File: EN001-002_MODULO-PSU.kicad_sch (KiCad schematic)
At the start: 90 parts, among them J1 2x5P 2.54mm, J2 Conn_01x02, J3 Barrel_Jack_Switch, J5 1x3P 2mm, J6 Conn_01x04, Q10 AO3401, Q11 KY6802, Q13 MMBT2222A, Q2 AO3401, Q3 KY6802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

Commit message: schematic minor rearrangments
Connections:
- net DRIVE: now also U2.4; no longer U2.5
- net RESET: now also U2.5; no longer U2.4
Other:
- moved on the sheet: U2B
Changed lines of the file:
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@@
 	(symbol
 		(lib_id "00EN_DB:IC_LOGIC/74HC132D,653")
-		(at 154.94 134.62 180)
+		(at 154.94 134.62 0)
+		(mirror y)
 		(unit 2)
 		(exclude_from_sim no)
@@
 		(dnp no)
 		(property "Reference" "U2"
-			(at 154.94 140.208 0)
+			(at 154.94 129.54 0)
 			(effects
 				(font
@@
 		)
 		(property "Value" "74HC132D,653"
-			(at 154.9483 140.97 0)
+			(at 154.9483 128.27 0)
 			(effects
 				(font
@@
 		)
 		(property "Datasheet" "http://www.ti.com/lit/gpn/sn74LS132"
-			(at 154.94 142.24 0)
+			(at 154.94 127 0)
 			(effects
 				(font
@@
 		)
 		(property "Sim.Library" "/home/fabio/Documents/03_KICAD_DEVELOPEMENT/EN_KICAD_LIBRARY/symbols/NAND_ST.cir"
-			(at 154.94 144.78 0)
+			(at 154.94 124.46 0)
 			(effects
 				(font
@@
 		)
 		(property "Sim.Name" "74HC132"
-			(at 146.05 149.86 0)
+			(at 146.05 119.38 0)
 			(effects
 				(font
@@
 		)
 		(property "Sim.Device" "SUBCKT"
-			(at 156.21 149.86 0)
+			(at 156.21 119.38 0)
 			(effects
 				(font
@@
 		)
 		(property "Sim.Pins" "1=1A 2=1B 3=1OUT 4=2A 5=2B 6=2OUT 7=AGND 8=3OUT 9=3A 10=3B 11=4OUT 12=4A 13=5B 14=VCC"
-			(at 153.67 147.32 0)
+			(at 153.67 121.92 0)
 			(effects
 				(font

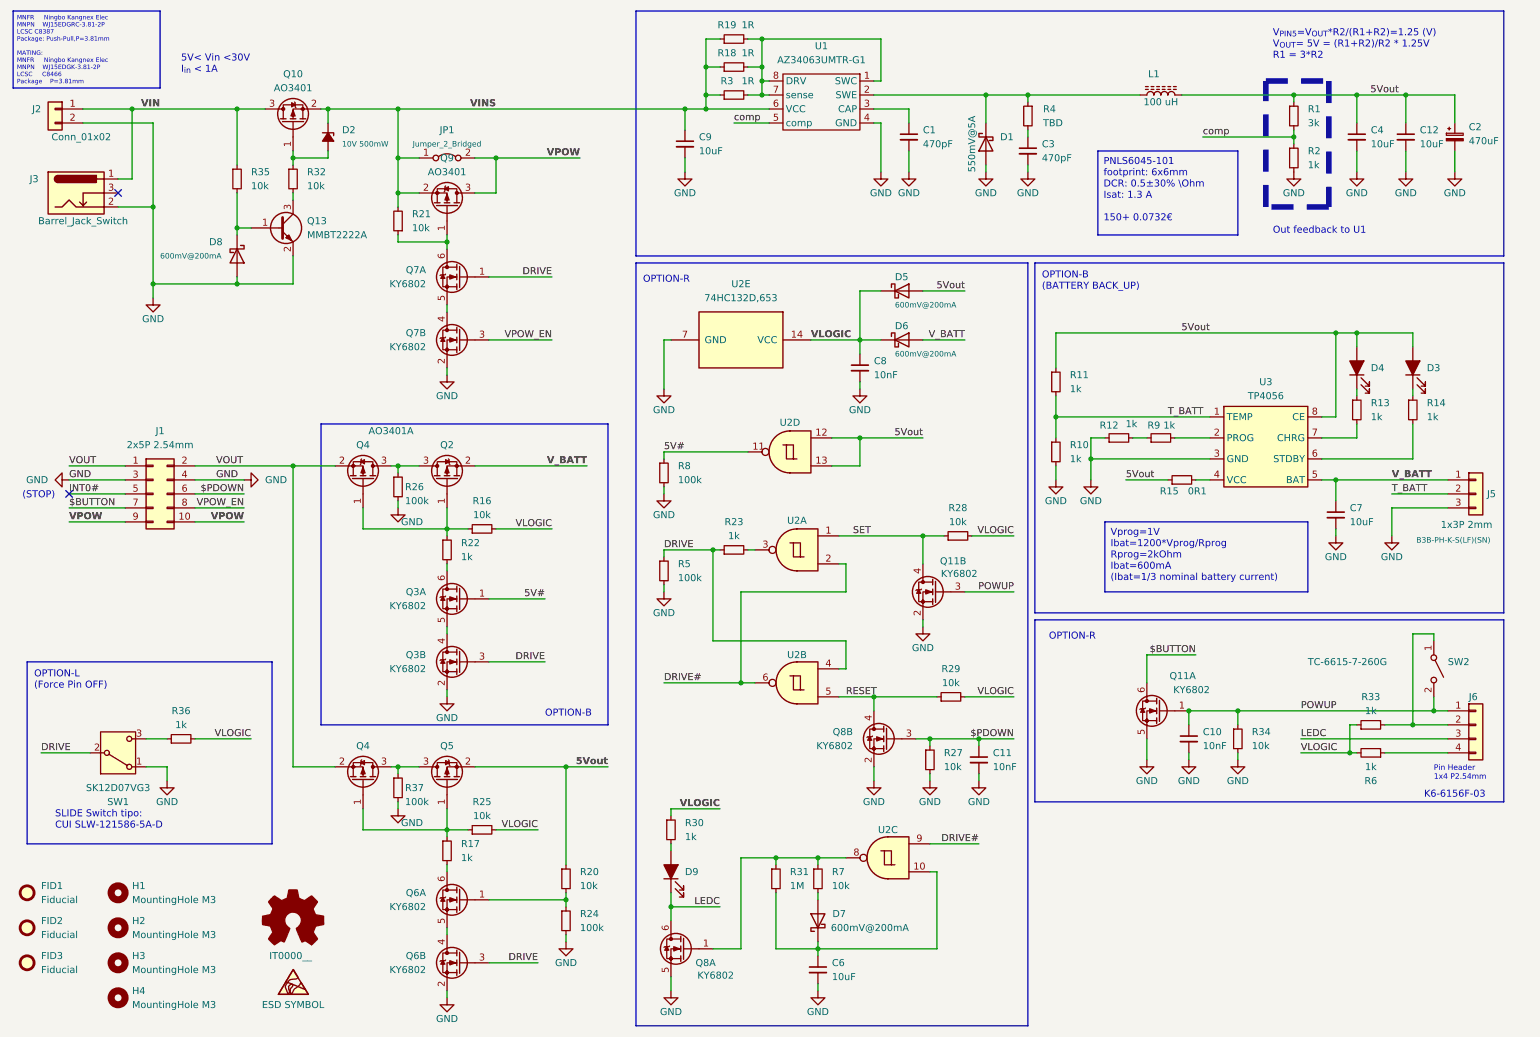
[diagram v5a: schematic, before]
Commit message: Adde Q12 to drive power-up from microcontroller
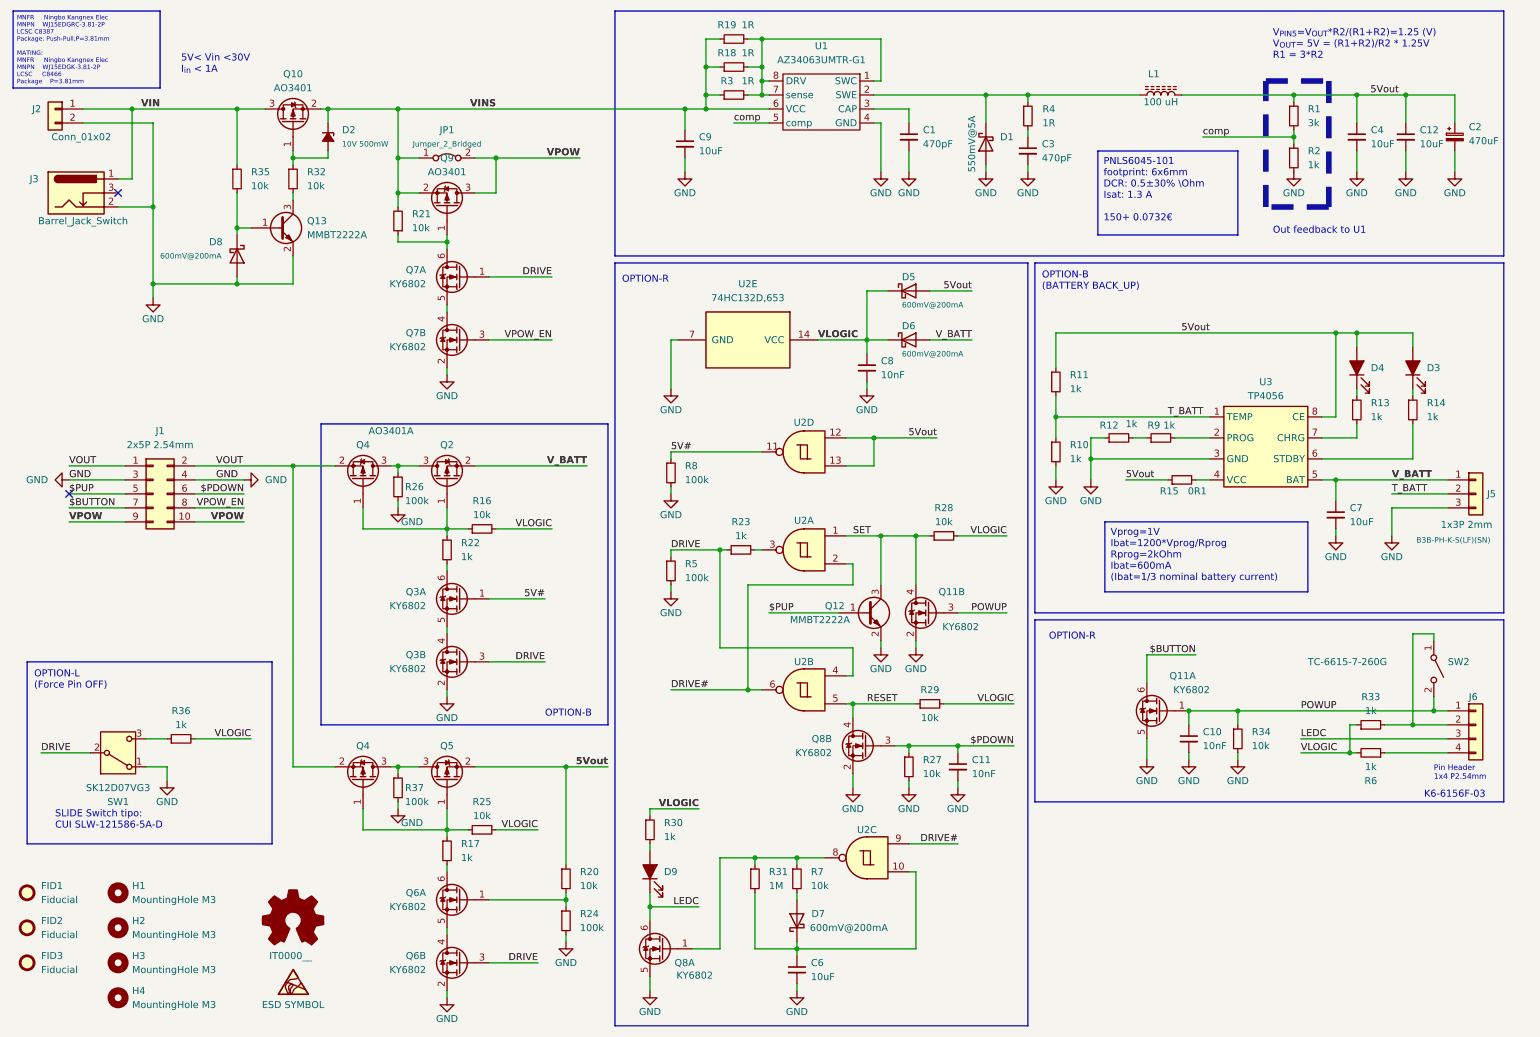
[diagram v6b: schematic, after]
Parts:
- removed R4: TBD, Resistor_SMD:R_0805_2012Metric_Pad1.20x1.40mm_HandSolder, symbol Device:R_Small
- added Q12: MMBT2222A, Package_TO_SOT_SMD:SOT-23, symbol 00EN_DB:MOSFET/MMBT2222A
- added R4: 1R, Resistor_SMD:R_0805_2012Metric_Pad1.20x1.40mm_HandSolder, symbol 00_EV_DATABASE:Res-SMD/0805_1R
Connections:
- net GND: now also Q12.2 (E)
- net SET: now also Q12.3 (C)
- net at C3.1: now also R4.2
- net at D1.1 (K), L1.1, U1.2 (SWE): now also R4.1
- net INT0# renamed $PUP
- net $PUP: now also Q12.1 (B)
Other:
- note removed: "(STOP)"
- moved on the sheet: C11, C6, C8, D5, D6, D7, D9, Q11B, Q8A, Q8B, R23, R27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
